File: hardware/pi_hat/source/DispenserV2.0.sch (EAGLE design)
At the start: 13 parts, among them J10 455-1750-1-ND, J11 455-1750-1-ND, J9 455-1750-1-ND, U2 A4988

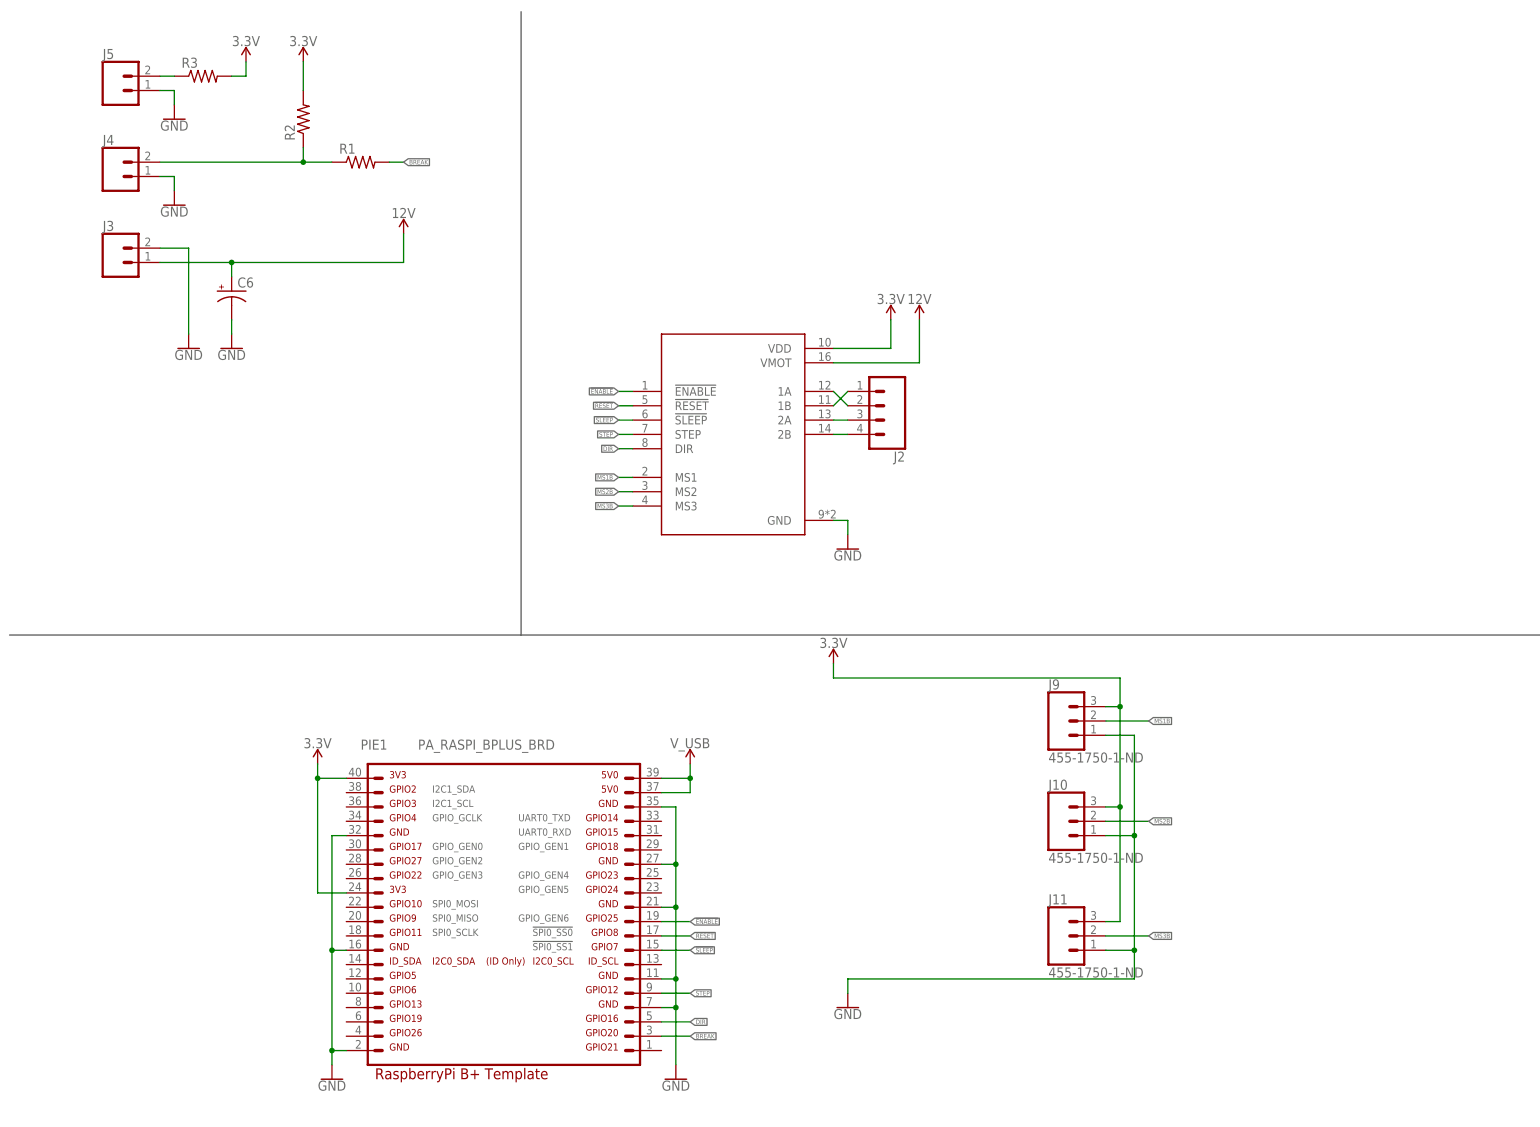
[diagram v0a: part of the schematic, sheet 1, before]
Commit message: Updating Pi Hat with changes for break sensor
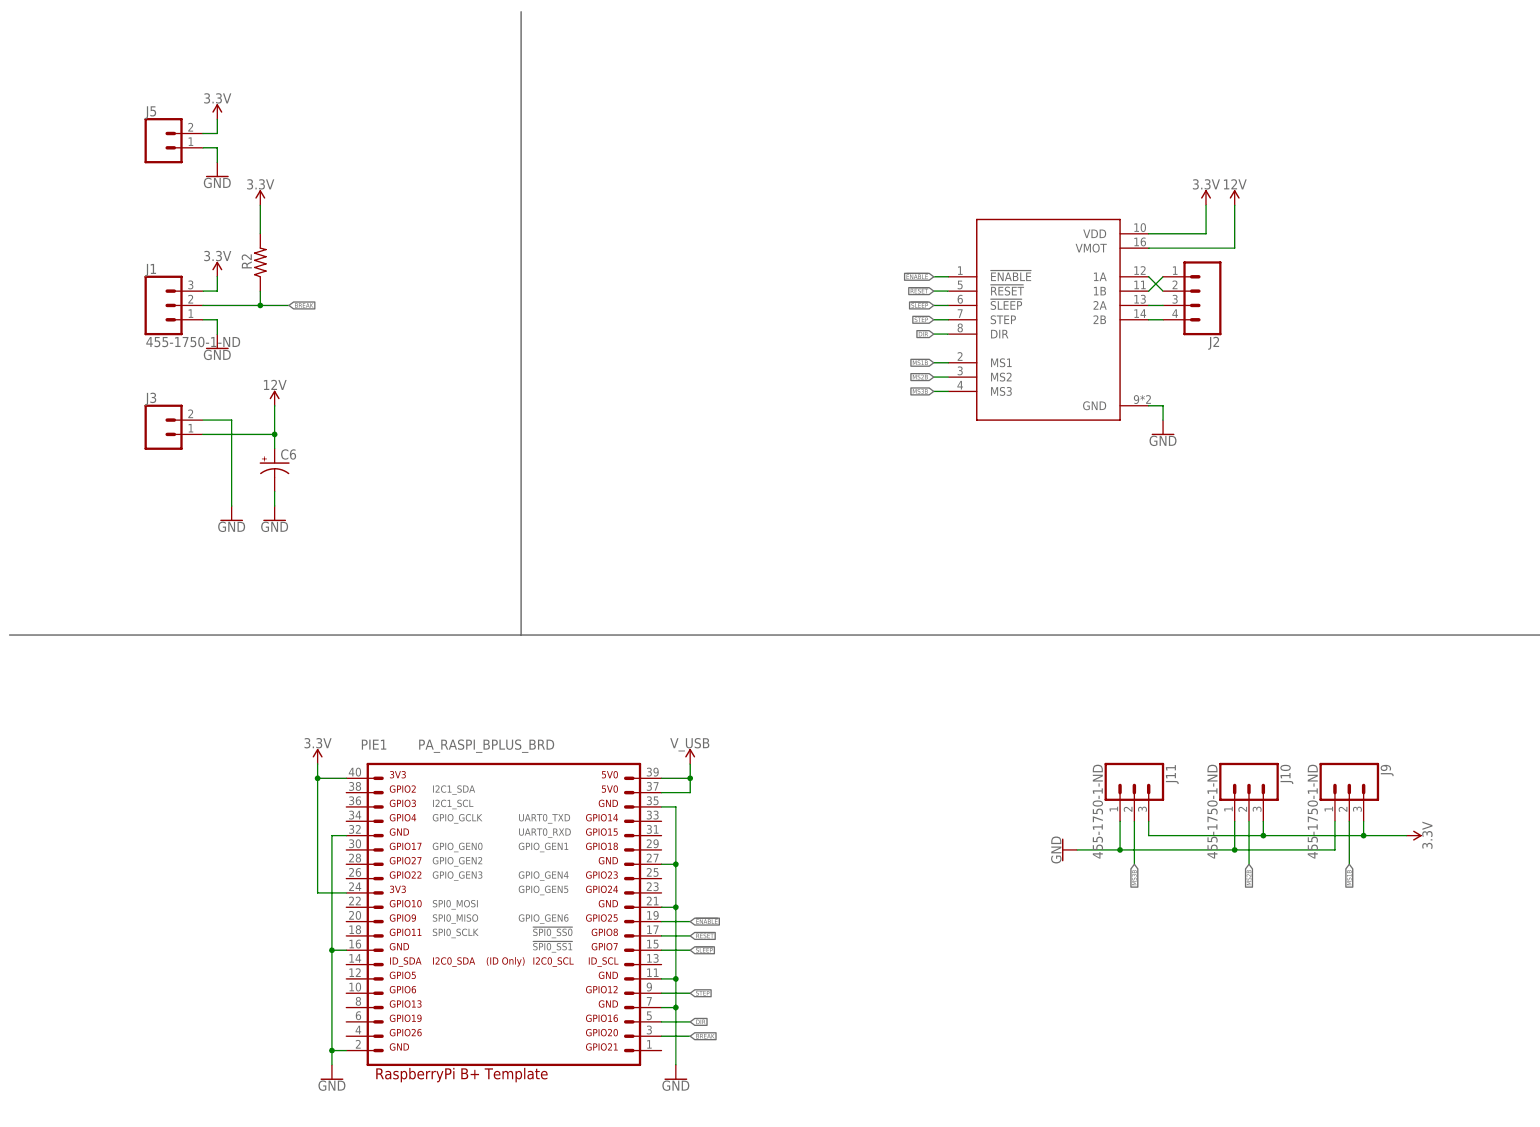
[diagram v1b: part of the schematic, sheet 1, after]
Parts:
- removed J4: (no value), SparkFun-Connectors:CONN_02
- removed R1, R3: (no value), adafruit:R-US_0207/10
- added J1: 455-1750-1-ND, SparkFun-Connectors:CONN_03
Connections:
- removed net N$1: J4.2, R1.1, R2.1
- removed net N$2: J5.2, R3.1
- net 3.3V: now also J1.3, J5.2; no longer R3.2
- net BREAK: now also J1.2, R2.1; no longer R1.2
- net GND: now also J1.1; no longer J4.1
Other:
- moved on the sheet: C6, J10, J11, J2, J3, J5, J9, R2

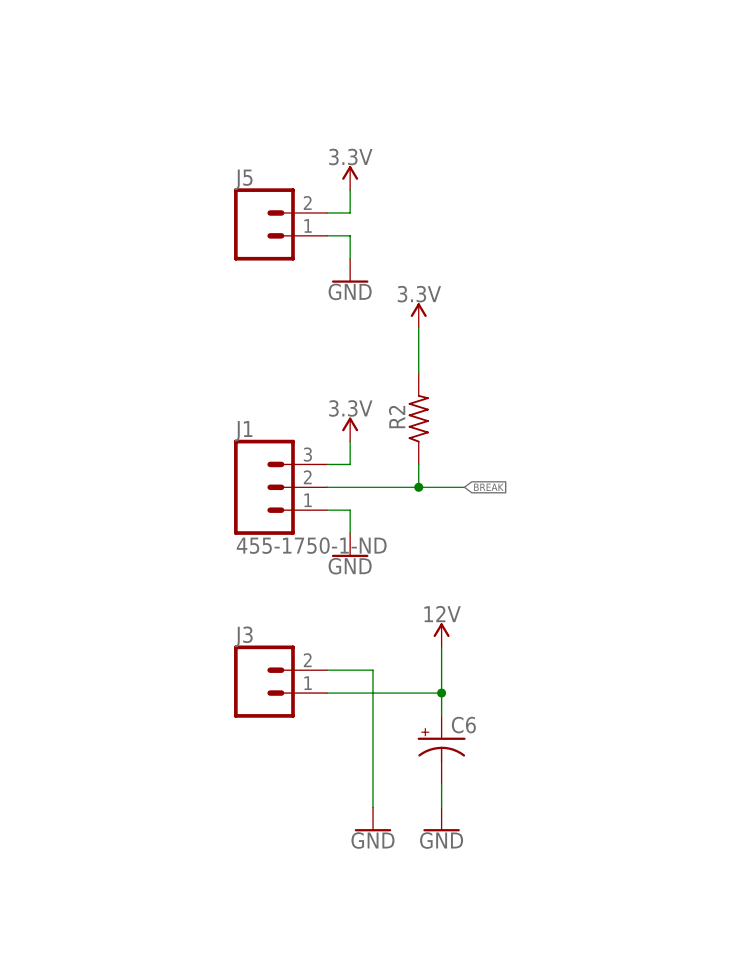
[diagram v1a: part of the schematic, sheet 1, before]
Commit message: Updated board to include connectors for break sensors
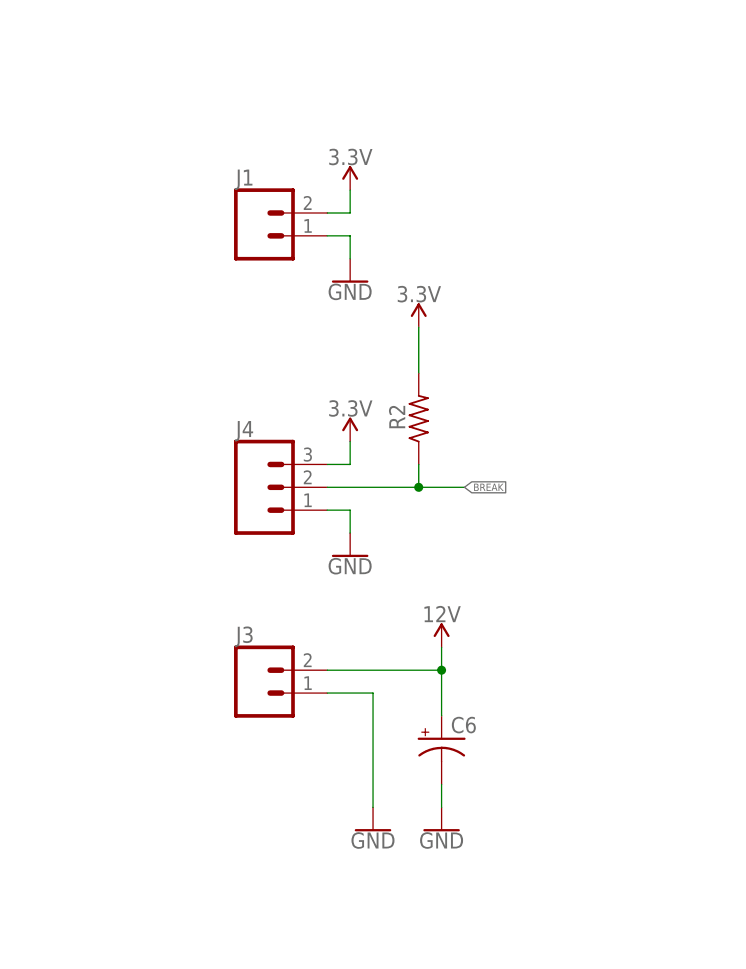
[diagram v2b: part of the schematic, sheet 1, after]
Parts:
- removed J5: (no value), SparkFun-Connectors:CONN_02
- added J4: (no value), SparkFun-Connectors:CONN_03SCREW
- J1: value 455-1750-1-ND -> (none); device SparkFun-Connectors:CONN_03 -> SparkFun-Connectors:CONN_023.5MM
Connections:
- net 12V: now also J3.2; no longer J3.1
- net 3.3V: now also J1.2, J4.3; no longer J1.3, J5.2
- net BREAK: now also J4.2; no longer J1.2
- net GND: now also J3.1, J4.1; no longer J3.2, J5.1
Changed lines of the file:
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@@
 <part name="GND2" library="SparkFun-PowerSymbols" deviceset="GND" device=""/>
 <part name="J2" library="SparkFun-Connectors" deviceset="CONN_04" device=""/>
-<part name="J5" library="SparkFun-Connectors" deviceset="CONN_02" device=""/>
 <part name="SUPPLY3" library="SparkFun-PowerSymbols" deviceset="3.3V" device=""/>
 <part name="GND1" library="SparkFun-PowerSymbols" deviceset="GND" device=""/>
@@
 <part name="SUPPLY5" library="SparkFun-PowerSymbols" deviceset="3.3V" device=""/>
 <part name="GND4" library="SparkFun-PowerSymbols" deviceset="GND" device=""/>
-<part name="J1" library="SparkFun-Connectors" deviceset="CONN_03" device="" value="455-1750-1-ND"/>
 <part name="SUPPLY6" library="SparkFun-PowerSymbols" deviceset="3.3V" device=""/>
+<part name="J4" library="SparkFun-Connectors" deviceset="CONN_03" device="SCREW"/>
+<part name="J1" library="SparkFun-Connectors" deviceset="CONN_02" device="3.5MM"/>
 </parts>
 <sheets>
@@
 <attribute name="NAME" x="218.44" y="154.432" size="1.778" layer="95" font="vector" rot="R180"/>
 </instance>
-<instance part="J5" gate="G$1" x="30.48" y="187.96" smashed="yes">
-<attribute name="VALUE" x="27.94" y="183.134" size="1.778" layer="96" font="vector"/>
-<attribute name="NAME" x="27.94" y="193.548" size="1.778" layer="95" font="vector"/>
-</instance>
 <instance part="SUPPLY3" gate="G$1" x="40.64" y="193.04" smashed="yes">
 <attribute name="VALUE" x="40.64" y="195.834" size="1.778" layer="96" align="bottom-center"/>
@@
 <attribute name="VALUE" x="40.64" y="152.146" size="1.778" layer="96" align="top-center"/>
 </instance>
-<instance part="J1" gate="J$1" x="30.48" y="160.02" smashed="yes">
+<instance part="SUPPLY6" gate="G$1" x="40.64" y="165.1" smashed="yes">
+<attribute name="VALUE" x="40.64" y="167.894" size="1.778" layer="96" align="bottom-center"/>
+</instance>
+<instance part="J4" gate="J$1" x="30.48" y="160.02" smashed="yes">
 <attribute name="VALUE" x="27.94" y="152.654" size="1.778" layer="96" font="vector"/>
 <attribute name="NAME" x="27.94" y="165.608" size="1.778" layer="95" font="vector"/>
 </instance>
-<instance part="SUPPLY6" gate="G$1" x="40.64" y="165.1" smashed="yes">
-<attribute name="VALUE" x="40.64" y="167.894" size="1.778" layer="96" align="bottom-center"/>
+<instance part="J1" gate="G$1" x="30.48" y="187.96" smashed="yes">
+<attribute name="VALUE" x="27.94" y="183.134" size="1.778" layer="96" font="vector"/>
+<attribute name="NAME" x="27.94" y="193.548" size="1.778" layer="95" font="vector"/>
 </instance>
 </instances>
@@
 </segment>
 <segment>
-<pinref part="J3" gate="G$1" pin="2"/>
-<pinref part="GND16" gate="1" pin="GND"/>
-<wire x1="38.1" y1="139.7" x2="43.18" y2="139.7" width="0.1524" layer="91"/>
-<wire x1="43.18" y1="139.7" x2="43.18" y2="124.46" width="0.1524" layer="91"/>
-</segment>
-<segment>
 <pinref part="C6" gate="G$1" pin="-"/>
 <pinref part="GND5" gate="1" pin="GND"/>
@@
 </segment>
 <segment>
-<pinref part="J5" gate="G$1" pin="1"/>
 <pinref part="GND1" gate="1" pin="GND"/>
 <wire x1="38.1" y1="187.96" x2="40.64" y2="187.96" width="0.1524" layer="91"/>
 <wire x1="40.64" y1="187.96" x2="40.64" y2="185.42" width="0.1524" layer="91"/>
+<pinref part="J1" gate="G$1" pin="1"/>
 </segment>
 <segment>
@@
 <pinref part="GND4" gate="1" pin="GND"/>
 <wire x1="40.64" y1="157.48" x2="40.64" y2="154.94" width="0.1524" layer="91"/>
-<pinref part="J1" gate="J$1" pin="1"/>
+<pinref part="J4" gate="J$1" pin="1"/>
+</segment>
+<segment>
+<pinref part="J3" gate="G$1" pin="1"/>
+<pinref part="GND16" gate="1" pin="GND"/>
+<wire x1="38.1" y1="137.16" x2="43.18" y2="137.16" width="0.1524" layer="91"/>
+<wire x1="43.18" y1="137.16" x2="43.18" y2="124.46" width="0.1524" layer="91"/>
 </segment>
 </net>
@@
 </segment>
 <segment>
-<pinref part="J5" gate="G$1" pin="2"/>
 <wire x1="38.1" y1="190.5" x2="40.64" y2="190.5" width="0.1524" layer="91"/>
 <pinref part="SUPPLY3" gate="G$1" pin="3.3V"/>
 <wire x1="40.64" y1="193.04" x2="40.64" y2="190.5" width="0.1524" layer="91"/>
-</segment>
-<segment>
-<pinref part="J1" gate="J$1" pin="3"/>
+<pinref part="J1" gate="G$1" pin="2"/>
+</segment>
+<segment>
 <wire x1="38.1" y1="162.56" x2="40.64" y2="162.56" width="0.1524" layer="91"/>
 <pinref part="SUPPLY6" gate="G$1" pin="3.3V"/>
 <wire x1="40.64" y1="162.56" x2="40.64" y2="165.1" width="0.1524" layer="91"/>
+<pinref part="J4" gate="J$1" pin="3"/>
 </segment>
 </net>
 <net name="12V" class="0">
 <segment>
-<pinref part="J3" gate="G$1" pin="1"/>
-<wire x1="38.1" y1="137.16" x2="50.8" y2="137.16" width="0.1524" layer="91"/>
 <pinref part="C6" gate="G$1" pin="+"/>
-<wire x1="50.8" y1="134.62" x2="50.8" y2="137.16" width="0.1524" layer="91"/>
-<junction x="50.8" y="137.16"/>
 <pinref part="SUPPLY1" gate="G$1" pin="12V"/>
-<wire x1="50.8" y1="142.24" x2="50.8" y2="137.16" width="0.1524" layer="91"/>
+<wire x1="50.8" y1="142.24" x2="50.8" y2="139.7" width="0.1524" layer="91"/>
+<pinref part="J3" gate="G$1" pin="2"/>
+<wire x1="50.8" y1="139.7" x2="50.8" y2="134.62" width="0.1524" layer="91"/>
+<wire x1="38.1" y1="139.7" x2="50.8" y2="139.7" width="0.1524" layer="91"/>
+<junction x="50.8" y="139.7"/>
 </segment>
 <segment>
@@
 <wire x1="48.26" y1="162.56" x2="48.26" y2="160.02" width="0.1524" layer="91"/>
 <junction x="48.26" y="160.02"/>
-<pinref part="J1" gate="J$1" pin="2"/>
-</segment>
-</net>
+<pinref part="J4" gate="J$1" pin="2"/>
+</segment>
+</net>

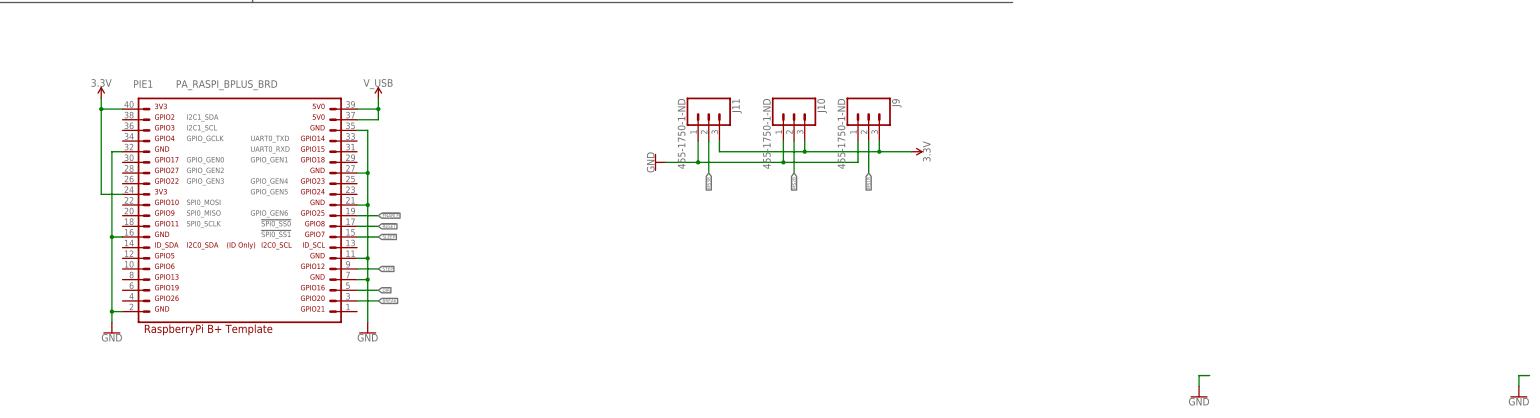
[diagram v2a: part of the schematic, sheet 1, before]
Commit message: Updated Pi HAT to fix the Pi header pinout
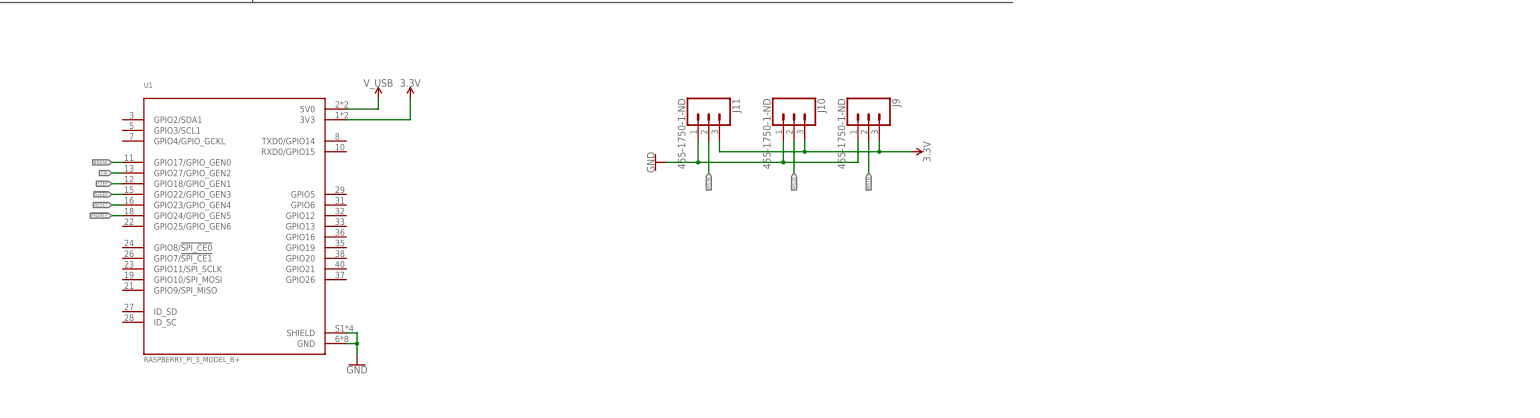
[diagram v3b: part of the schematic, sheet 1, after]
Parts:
- removed PIE1: PA_RASPI_BPLUS_BRD, PatternAgents-Boards:PA_RASPI_BPLUS_BRD
- added U1: RASPBERRY_PI_3_MODEL_B+, RASPBERRY_PI_3_MODEL_B_:RASPBERRY_PI_3_MODEL_B+
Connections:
- net !ENABLE: now also U1.GPIO24/GPIO_GEN5; no longer PIE1.19
- net !RESET: now also U1.GPIO23/GPIO_GEN4; no longer PIE1.17
- net !SLEEP: now also U1.GPIO22/GPIO_GEN3; no longer PIE1.15
- net 3.3V: now also U1.3V3; no longer PIE1.24, PIE1.40
- net BREAK: now also U1.GPIO17/GPIO_GEN0; no longer PIE1.3
- net DIR: now also U1.GPIO27/GPIO_GEN2; no longer PIE1.5
- net GND: now also U1.GND, U1.SHIELD; no longer PIE1.11, PIE1.16, PIE1.2, PIE1.21, PIE1.27, PIE1.32, PIE1.35, PIE1.7
- net STEP: now also U1.GPIO18/GPIO_GEN1; no longer PIE1.9
- net V_USB: now also U1.5V0; no longer PIE1.37, PIE1.39
